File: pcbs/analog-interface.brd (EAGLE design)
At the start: 76.9 x 13.5 mm, 29 parts, among them U1 ISL3179EIBZ, U2 ATMEGA328P

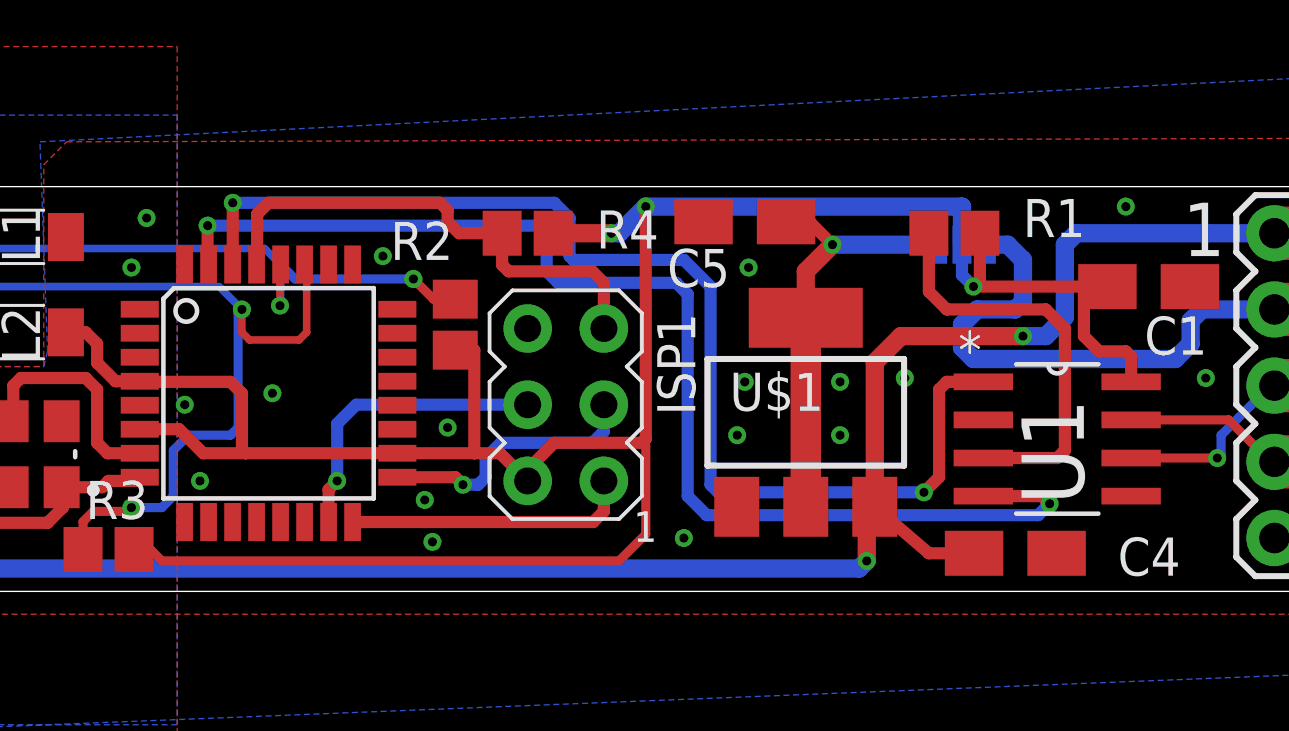
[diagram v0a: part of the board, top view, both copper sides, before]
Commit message: Now has control of Tx/Rx for RS485 chip
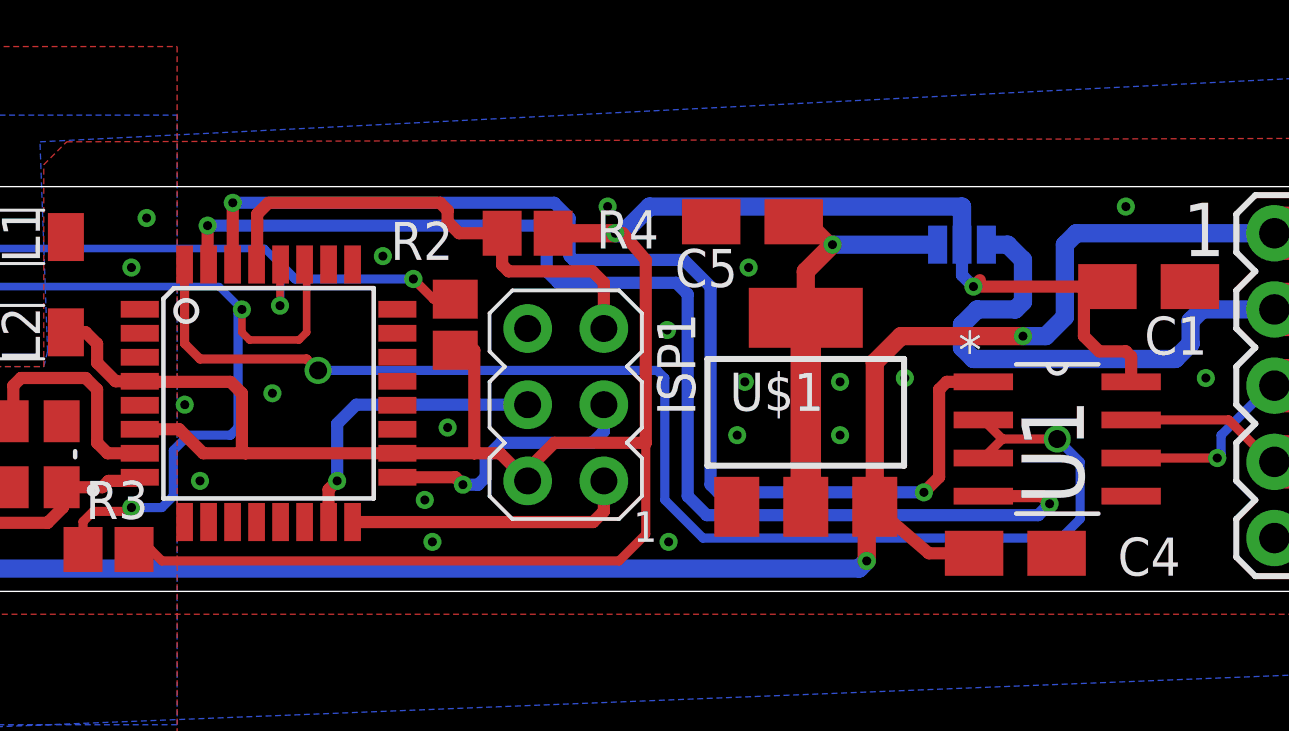
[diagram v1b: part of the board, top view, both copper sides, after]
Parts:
- removed R1: 1k, resistor:R0805
- moved C5 0.25 mm to (21.0, 12.8)
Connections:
- removed net N$1: R1.1, U1.3
- new net TXEN: U1.2, U1.3, U2.32
- net GND: no longer U1.2
- net VCC: no longer R1.2
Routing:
- net TXEN: track 0.00 -> 44.4 mm, vias 0 -> 2
- net N$1: track 13.9 -> 0.00 mm
- net VCC: track 88.3 -> 86.4 mm, vias 3 -> 2
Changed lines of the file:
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@@
 <?xml version="1.0" encoding="utf-8"?>
 <!DOCTYPE eagle SYSTEM "eagle.dtd">
-<eagle version="6.5.0">
+<eagle version="6.6.0">
 <drawing>
 <settings>
@@
 <attribute name="NAME" x="36.113" y="9.668" size="1.27" layer="25" rot="R180"/>
 </element>
-<element name="R1" library="resistor" package="R0805" value="1k" x="27.686" y="12.446" smashed="yes">
-<attribute name="NAME" x="29.972" y="12.319" size="1.27" layer="25"/>
-</element>
 <element name="ISP1" library="adafruit" package="AVRISP" value="AVRISP-6" x="14.732" y="6.731" rot="R180"/>
 <element name="U2" library="SparkFun-DigitalIC" package="TQFP32-08" value="ATMEGA328P" x="4.826" y="7.112" smashed="yes">
@@
 <attribute name="NAME" x="35.224" y="2.302" size="1.27" layer="25" rot="R180"/>
 </element>
-<element name="C5" library="resistor" package="A/3216-18R" value="22uF" x="20.701" y="12.827" smashed="yes">
-<attribute name="NAME" x="18.116" y="10.652" size="1.27" layer="25"/>
+<element name="C5" library="resistor" package="A/3216-18R" value="22uF" x="20.955" y="12.827" smashed="yes">
+<attribute name="NAME" x="18.37" y="10.652" size="1.27" layer="25"/>
 </element>
 <element name="JP9" library="SparkFun-Passives" package="SJ_3_PASTE1&amp;2" value="JUMPER-31-2" x="27.94" y="12.065" rot="MR0"/>
@@
 <signal name="GND">
 <contactref element="U1" pad="5"/>
-<contactref element="U1" pad="2"/>
 <contactref element="ISP1" pad="6"/>
 <contactref element="C1" pad="-"/>
@@
 <via x="20.447" y="5.715" extent="1-16" drill="0.3" shape="square"/>
 <via x="23.876" y="5.715" extent="1-16" drill="0.3" shape="square"/>
-<via x="18.669" y="2.286" extent="1-16" drill="0.3" shape="square"/>
+<via x="18.161" y="2.159" extent="1-16" drill="0.3" shape="square"/>
 <via x="-4.699" y="7.62" extent="1-16" drill="0.3" shape="square"/>
 <via x="2.032" y="6.731" extent="1-16" drill="0.3" shape="square"/>
@@
 <via x="0.254" y="11.303" extent="1-16" drill="0.3" shape="square"/>
 <via x="0.762" y="12.954" extent="1-16" drill="0.3" shape="square"/>
+<via x="16.129" y="13.335" extent="1-16" drill="0.3" shape="square"/>
+<via x="18.1102" y="9.2202" extent="1-16" drill="0.3" shape="square"/>
+<wire x1="0.5334" y1="8.312" x2="0.5334" y2="6.712" width="0" layer="19" extent="1-1"/>
+<wire x1="0.254" y1="11.303" x2="0.5334" y2="8.312" width="0" layer="19" extent="1-1"/>
 </signal>
 <signal name="VCC">
 <contactref element="ISP1" pad="2"/>
 <contactref element="U1" pad="8"/>
-<contactref element="R1" pad="2"/>
 <contactref element="U2" pad="4"/>
 <contactref element="U2" pad="6"/>
@@
 <wire x1="11.684" y1="5.112" x2="12.541" y2="5.112" width="0.4064" layer="1"/>
 <wire x1="12.541" y1="5.112" x2="13.462" y2="4.191" width="0.4064" layer="1"/>
-<wire x1="14.312" y1="12.446" x2="16.256" y2="12.446" width="0.6096" layer="1"/>
-<via x="16.256" y="12.446" extent="1-16" drill="0.3"/>
-<wire x1="16.256" y1="12.446" x2="16.51" y2="12.446" width="0.6096" layer="16"/>
-<wire x1="16.51" y1="12.446" x2="17.399" y2="13.335" width="0.6096" layer="16"/>
-<wire x1="17.399" y1="13.335" x2="27.94" y2="13.335" width="0.6096" layer="16"/>
+<wire x1="14.312" y1="12.446" x2="16.383" y2="12.446" width="0.6096" layer="1"/>
+<via x="16.383" y="12.446" extent="1-16" drill="0.3"/>
+<wire x1="16.383" y1="12.446" x2="16.637" y2="12.446" width="0.6096" layer="16"/>
+<wire x1="16.637" y1="12.446" x2="17.526" y2="13.335" width="0.6096" layer="16"/>
+<wire x1="17.526" y1="13.335" x2="27.94" y2="13.335" width="0.6096" layer="16"/>
 <wire x1="27.94" y1="13.335" x2="27.94" y2="12.065" width="0.6096" layer="16"/>
-<wire x1="28.536" y1="12.446" x2="28.536" y2="10.883" width="0.4064" layer="1"/>
 <wire x1="28.536" y1="10.883" x2="28.321" y2="10.668" width="0.4064" layer="1"/>
-<via x="17.399" y="13.335" extent="1-16" drill="0.3"/>
 <wire x1="13.462" y1="4.191" x2="13.462" y2="4.572" width="0.8128" layer="1"/>
 <wire x1="13.462" y1="4.572" x2="14.351" y2="5.461" width="0.4064" layer="1"/>
@@
 <wire x1="-0.889" y1="8.763" x2="-1.27" y2="9.144" width="0.4064" layer="1"/>
 <wire x1="-1.27" y1="9.144" x2="-1.929" y2="9.144" width="0.4064" layer="1"/>
-<wire x1="17.399" y1="13.335" x2="17.399" y2="5.588" width="0.4064" layer="1"/>
-<wire x1="17.399" y1="5.588" x2="17.272" y2="5.461" width="0.4064" layer="1"/>
+<wire x1="17.399" y1="11.557" x2="17.399" y2="5.461" width="0.4064" layer="1"/>
+<wire x1="17.399" y1="5.461" x2="17.272" y2="5.461" width="0.4064" layer="1"/>
 <wire x1="0.5524" y1="7.493" x2="3.556" y2="7.493" width="0.4064" layer="1"/>
 <wire x1="3.556" y1="7.493" x2="3.937" y2="7.112" width="0.4064" layer="1"/>
@@
 <wire x1="1.27" y1="1.524" x2="16.51" y2="1.524" width="0.3048" layer="1"/>
 <wire x1="16.51" y1="1.524" x2="17.399" y2="2.413" width="0.3048" layer="1"/>
+<wire x1="16.383" y1="12.446" x2="16.637" y2="12.446" width="0.4064" layer="1"/>
+<wire x1="16.637" y1="12.446" x2="17.399" y2="11.557" width="0.4064" layer="1"/>
 </signal>
 <signal name="485_P" class="1">
@@
 <wire x1="2.794" y1="12.7" x2="2.794" y2="11.4366" width="0.4064" layer="1"/>
 <wire x1="2.794" y1="11.4366" x2="2.826" y2="11.4046" width="0.4064" layer="1"/>
-</signal>
-<signal name="N$1">
-<contactref element="U1" pad="3"/>
-<contactref element="R1" pad="1"/>
-<wire x1="26.836" y1="12.446" x2="26.836" y2="10.502" width="0.4064" layer="1"/>
-<wire x1="26.836" y1="10.502" x2="27.432" y2="9.906" width="0.4064" layer="1"/>
-<wire x1="27.432" y1="9.906" x2="30.734" y2="9.906" width="0.4064" layer="1"/>
-<wire x1="30.734" y1="9.906" x2="31.369" y2="9.271" width="0.4064" layer="1"/>
-<wire x1="31.369" y1="9.271" x2="31.369" y2="5.207" width="0.4064" layer="1"/>
-<wire x1="31.369" y1="5.207" x2="31.115" y2="4.953" width="0.4064" layer="1"/>
-<wire x1="31.115" y1="4.953" x2="28.6512" y2="4.953" width="0.4064" layer="1"/>
 </signal>
 <signal name="!RESET">
@@
 <wire x1="23.622" y1="12.065" x2="27.1272" y2="12.065" width="0.6096" layer="16"/>
 <wire x1="22.733" y1="9.627" x2="22.733" y2="3.327" width="1.016" layer="1"/>
-<wire x1="22.076" y1="12.827" x2="22.86" y2="12.827" width="0.4064" layer="1"/>
+<wire x1="22.33" y1="12.827" x2="22.86" y2="12.827" width="0.4064" layer="1"/>
 <wire x1="22.86" y1="12.827" x2="23.622" y2="12.065" width="0.4064" layer="1"/>
 </signal>
@@
 <wire x1="-26.924" y1="7.112" x2="-31.242" y2="7.112" width="0.6096" layer="16"/>
 </signal>
+<signal name="TXEN">
+<contactref element="U1" pad="3"/>
+<contactref element="U1" pad="2"/>
+<contactref element="U2" pad="32"/>
+<wire x1="2.026" y1="11.4046" x2="2.026" y2="8.769" width="0.3048" layer="1"/>
+<wire x1="2.026" y1="8.769" x2="2.54" y2="8.255" width="0.3048" layer="1"/>
+<wire x1="2.54" y1="8.255" x2="6.096" y2="8.255" width="0.3048" layer="1"/>
+<wire x1="6.096" y1="8.255" x2="6.477" y2="7.874" width="0.3048" layer="1"/>
+<via x="6.477" y="7.874" extent="1-16" drill="0.6"/>
+<wire x1="6.477" y1="7.874" x2="17.78" y2="7.874" width="0.3048" layer="16"/>
+<wire x1="17.78" y1="7.874" x2="18.034" y2="7.62" width="0.3048" layer="16"/>
+<wire x1="18.034" y1="7.62" x2="18.034" y2="3.556" width="0.3048" layer="16"/>
+<wire x1="18.034" y1="3.556" x2="19.304" y2="2.286" width="0.3048" layer="16"/>
+<wire x1="19.304" y1="2.286" x2="31.242" y2="2.286" width="0.3048" layer="16"/>
+<wire x1="31.242" y1="2.286" x2="31.877" y2="2.921" width="0.3048" layer="16"/>
+<wire x1="31.877" y1="2.921" x2="31.877" y2="4.826" width="0.3048" layer="16"/>
+<wire x1="31.877" y1="4.826" x2="31.115" y2="5.588" width="0.3048" layer="16"/>
+<via x="31.115" y="5.588" extent="1-16" drill="0.6"/>
+<wire x1="31.115" y1="5.588" x2="29.2862" y2="5.588" width="0.3048" layer="1"/>
+<wire x1="29.2862" y1="5.588" x2="28.6512" y2="4.953" width="0.3048" layer="1"/>
+<wire x1="28.6512" y1="6.223" x2="29.2862" y2="5.588" width="0.3048" layer="1"/>
+</signal>
 </signals>
